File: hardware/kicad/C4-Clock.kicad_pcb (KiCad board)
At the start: 2 copper layers, 99 x 99 mm, 39 parts, among them J1 Keypad, J2 Battery, J3 LCD1602, J4 Boost Module, J5 ICSP, K1 FINDER-36.11-5V, Q1 S9014, Q2 S9014, Q3 S9014, SW1 SW_SPST, SW2 SW_SPST, U1 ATmega328P-P, U2 AMS1117-5.0, U3 PCF8574A, U4 DS1302+, Y1 16MHz, Y2 32.768kHz

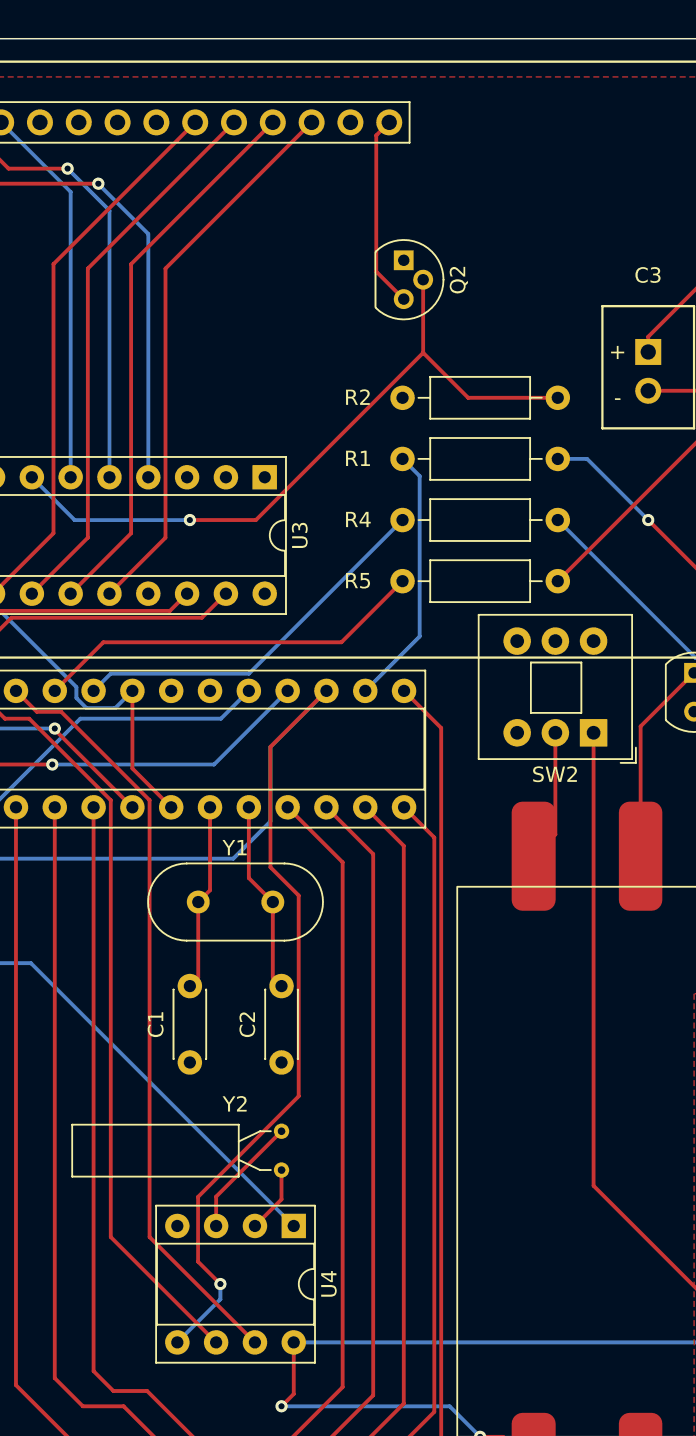
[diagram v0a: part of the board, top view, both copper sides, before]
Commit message: kicad: Remove unused pin A0
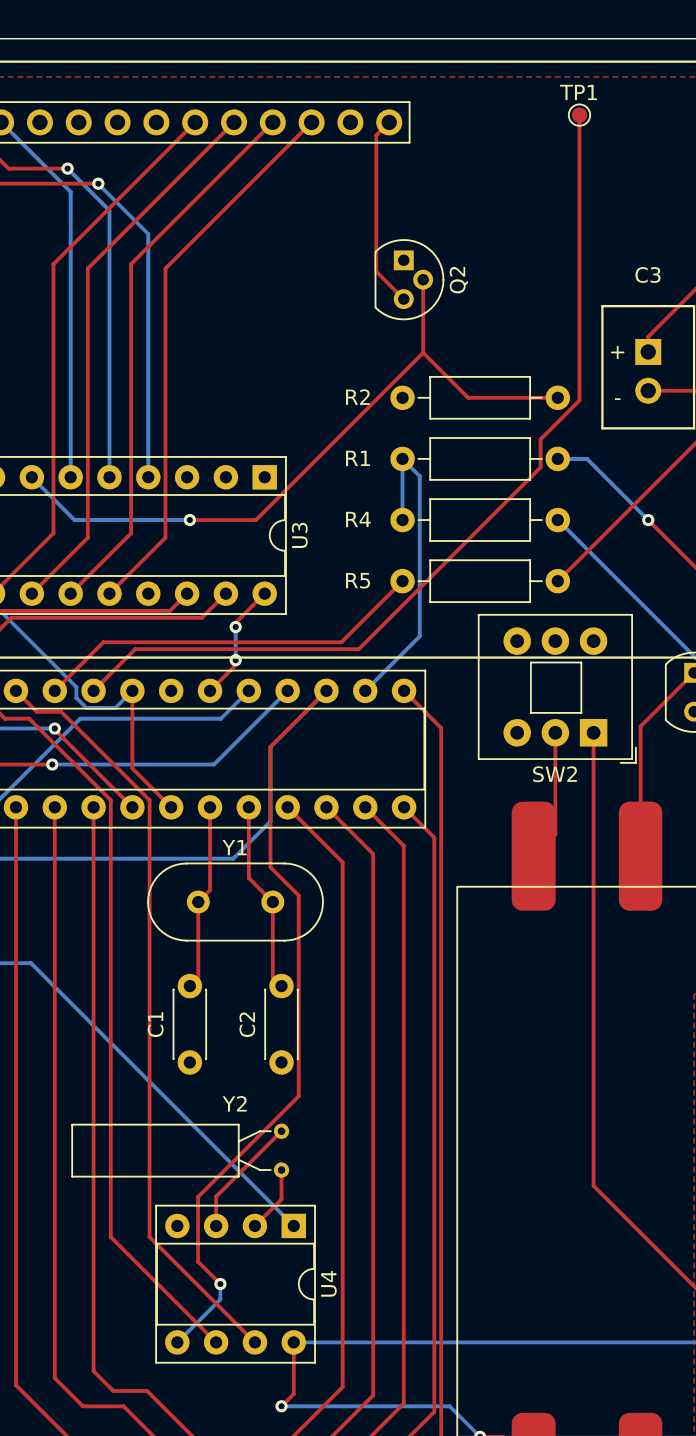
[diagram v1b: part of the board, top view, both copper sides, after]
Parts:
- added TP1: RandomSeed, TestPoint:TestPoint_Pad_D1.0mm, F.Cu at (144.5, 44.5)
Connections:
- R4 pad 1: LED -> BUZZER
- U1 pad 23: LED -> Net-(TP1-Pad1)
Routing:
- net Net-(TP1-Pad1): track 0.00 -> 61.0 mm
- net LED: track 24.9 -> 0.00 mm
- net +5V: track 111.8 -> 119.6 mm, vias 4 -> 6
- net BUZZER: track 17.1 -> 21.1 mm
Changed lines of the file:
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@@
   (net 35 "Net-(Q2-Pad2)")
   (net 36 "BUZZER")
-  (net 37 "LED")
+  (net 37 "Net-(TP1-Pad1)")
   (net 38 "Net-(SW1-Pad2)")
   (net 39 "Net-(BT1-Pad1)")
@@
     (fp_line (start 8.23 1.25) (end 8.23 -1.25) (layer "F.Fab") (width 0.1))
     (pad "1" thru_hole circle (at 0 0) (size 1.6 1.6) (drill 0.8) (layers *.Cu *.Mask)
-      (net 37 "LED") (pintype "passive"))
+      (net 36 "BUZZER") (pintype "passive"))
     (pad "2" thru_hole oval (at 10.16 0) (size 1.6 1.6) (drill 0.8) (layers *.Cu *.Mask)
       (net 7 "Net-(D1-Pad2)") (pintype "passive"))
@@
       (net 3 "GND") (pinfunction "GND") (pintype "passive"))
     (pad "23" thru_hole oval (at 7.62 12.7 90) (size 1.6 1.6) (drill 0.8) (layers *.Cu *.Mask)
-      (net 37 "LED") (pinfunction "PC0") (pintype "bidirectional"))
+      (net 37 "Net-(TP1-Pad1)") (pinfunction "PC0") (pintype "bidirectional"))
     (pad "24" thru_hole oval (at 7.62 10.16 90) (size 1.6 1.6) (drill 0.8) (layers *.Cu *.Mask)
       (net 8 "RELAY") (pinfunction "PC1") (pintype "bidirectional"))
@@
       (rotate (xyz 0 0 0))
     )
+  )
+  (footprint "TestPoint:TestPoint_Pad_D1.0mm" (layer "F.Cu")
+    (at 144.5 44.5)
+    (descr "SMD pad as test Point, diameter 1.0mm")
+    (tags "test point SMD pad")
+    (property "Sheetfile" "C4-Clock.kicad_sch")
+    (property "Sheetname" "")
+    (attr exclude_from_pos_files)
+    (fp_text reference "TP1" (at 0 -1.448) (layer "F.SilkS")
+      (effects (font (size 1 1) (thickness 0.15)))
+    )
+    (fp_text value "RandomSeed" (at 0 1.55) (layer "F.Fab")
+      (effects (font (size 1 1) (thickness 0.15)))
+    )
+    (fp_text user "${REFERENCE}" (at 0 -1.45) (layer "F.Fab")
+      (effects (font (size 1 1) (thickness 0.15)))
+    )
+    (fp_circle (center 0 0) (end 0 0.7) (layer "F.SilkS") (width 0.12) (fill none))
+    (fp_circle (center 0 0) (end 1 0) (layer "F.CrtYd") (width 0.05) (fill none))
+    (pad "1" smd circle (at 0 0) (size 1 1) (layers "F.Cu" "F.Mask")
+      (net 37 "Net-(TP1-Pad1)") (pinfunction "1") (pintype "passive"))
   )
   (footprint "Potentiometer_THT:Potentiometer_Vishay_T73YP_Vertical" (layer "F.Cu")
@@
   (segment (start 162.824511 118.705738) (end 158.530249 123) (width 0.25) (layer "F.Cu") (net 1))
   (segment (start 138 131) (end 139.5 131) (width 0.25) (layer "F.Cu") (net 1))
+  (segment (start 122 80.17402) (end 122 80.5) (width 0.25) (layer "F.Cu") (net 1))
+  (segment (start 122 77.72) (end 122 78) (width 0.25) (layer "F.Cu") (net 1))
   (segment (start 110.16 84.72) (end 110.16 84.645102) (width 0.25) (layer "F.Cu") (net 1))
+  (segment (start 122 80.5) (end 120.32 82.18) (width 0.25) (layer "F.Cu") (net 1))
   (segment (start 139.5 131) (end 141.5 133) (width 0.25) (layer "F.Cu") (net 1))
   (segment (start 125.8 128.2) (end 125 129) (width 0.25) (layer "F.Cu") (net 1))
   (segment (start 162.824511 99.624511) (end 162.824511 118.705738) (width 0.25) (layer "F.Cu") (net 1))
   (segment (start 158.530249 123) (end 155 123) (width 0.25) (layer "F.Cu") (net 1))
+  (segment (start 123.9 75.82) (end 122 77.72) (width 0.25) (layer "F.Cu") (net 1))
   (segment (start 162.2 99) (end 162.824511 99.624511) (width 0.25) (layer "F.Cu") (net 1))
   (segment (start 115.24 89.8) (end 110.16 84.72) (width 0.25) (layer "F.Cu") (net 1))
   (via (at 125 129) (size 0.8) (drill 0.4) (layers "F.Cu" "B.Cu") (net 1))
+  (via (at 122 80.17402) (size 0.8) (drill 0.4) (layers "F.Cu" "B.Cu") (net 1))
+  (via (at 122 78) (size 0.8) (drill 0.4) (layers "F.Cu" "B.Cu") (net 1))
   (via (at 138 131) (size 0.8) (drill 0.4) (layers "F.Cu" "B.Cu") (net 1))
   (via (at 110.16 84.645102) (size 0.8) (drill 0.4) (layers "F.Cu" "B.Cu") (net 1))
@@
   (segment (start 110.16 84.645102) (end 90.145102 84.645102) (width 0.25) (layer "B.Cu") (net 1))
   (segment (start 90.145102 84.645102) (end 88.5 83) (width 0.25) (layer "B.Cu") (net 1))
+  (segment (start 122 78) (end 122 80.17402) (width 0.25) (layer "B.Cu") (net 1))
   (segment (start 155 123) (end 153.18 124.82) (width 0.25) (layer "B.Cu") (net 1))
   (segment (start 154.34 83.54) (end 169.8 99) (width 0.25) (layer "B.Cu") (net 2))
@@
   (segment (start 134.044511 68.124511) (end 134.044511 78.615489) (width 0.25) (layer "B.Cu") (net 36))
   (segment (start 134.044511 78.615489) (end 130.48 82.18) (width 0.25) (layer "B.Cu") (net 36))
+  (segment (start 132.92 67) (end 132.92 71) (width 0.25) (layer "B.Cu") (net 36))
   (segment (start 132.92 67) (end 134.044511 68.124511) (width 0.25) (layer "B.Cu") (net 36))
-  (segment (start 122.864511 81.055489) (end 132.92 71) (width 0.25) (layer "B.Cu") (net 37))
-  (segment (start 113.824511 81.055489) (end 122.864511 81.055489) (width 0.25) (layer "B.Cu") (net 37))
+  (segment (start 144.5 45) (end 144.5 44.5) (width 0.25) (layer "F.Cu") (net 37))
+  (segment (start 115.43048 79.44952) (end 130.06078 79.44952) (width 0.25) (layer "F.Cu") (net 37))
+  (segment (start 144.5 63.1703) (end 144.5 45) (width 0.25) (layer "F.Cu") (net 37))
+  (segment (start 141.955489 65.714811) (end 144.5 63.1703) (width 0.25) (layer "F.Cu") (net 37))
+  (segment (start 141.955489 67.554811) (end 141.955489 65.714811) (width 0.25) (layer "F.Cu") (net 37))
+  (segment (start 130.06078 79.44952) (end 141.955489 67.554811) (width 0.25) (layer "F.Cu") (net 37))
+  (segment (start 112.7 82.18) (end 115.43048 79.44952) (width 0.25) (layer "F.Cu") (net 37))
   (segment (start 112.7 82.18) (end 113.824511 81.055489) (width 0.25) (layer "B.Cu") (net 37))
   (segment (start 86.6425 68.0925) (end 94.85 76.3) (width 0.25) (layer "F.Cu") (net 38))
@@
   (segment (start 121.840489 93.159511) (end 124.275489 90.724511) (width 0.25) (layer "B.Cu") (net 45))
   (segment (start 108.99048 83.55048) (end 110.58078 83.55048) (width 0.25) (layer "F.Cu") (net 46))
-  (segment (start 116.364511 117.924511) (end 123.26 124.82) (width 0.25) (layer "F.Cu") (net 46))
+  (segment (start 123.26 124.82) (end 116.364511 117.924511) (width 0.25) (layer "F.Cu") (net 46))
   (segment (start 107.62 82.18) (end 108.99048 83.55048) (width 0.25) (layer "F.Cu") (net 46))
   (segment (start 116.364511 89.334211) (end 116.364511 117.924511) (width 0.25) (layer "F.Cu") (net 46))

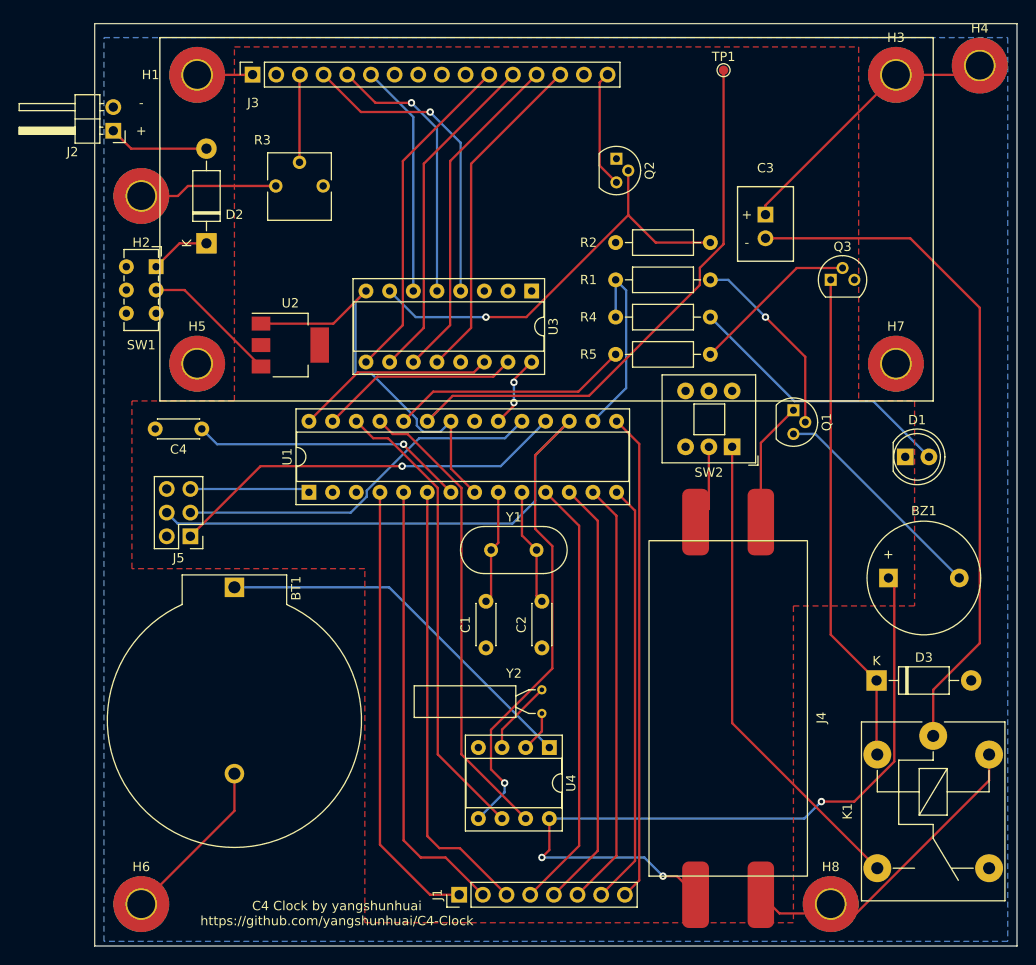
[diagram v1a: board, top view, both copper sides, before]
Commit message: kicad: Change ATmega328P to ESP32-WROOM-32
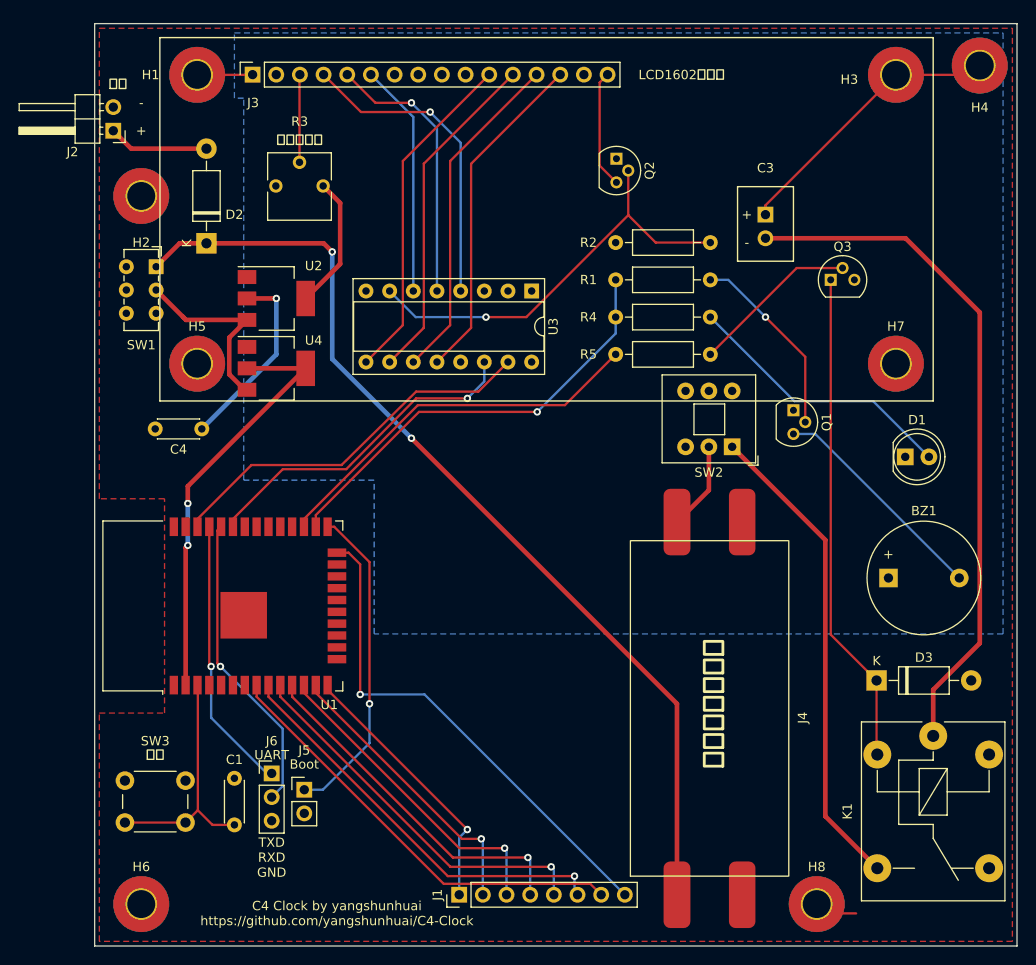
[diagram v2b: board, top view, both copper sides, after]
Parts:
- removed BT1: CR2032, Battery:BatteryHolder_ComfortableElectronic_CH273-2450_1x2450
- removed C2: 22pF, Capacitor_THT:C_Disc_D4.3mm_W1.9mm_P5.00mm
- removed TP1: RandomSeed, TestPoint:TestPoint_Pad_D1.0mm
- removed Y1: 16MHz, Crystal:Crystal_HC49-4H_Vertical
- removed Y2: 32.768kHz, Crystal:Crystal_AT310_D3.0mm_L10.0mm_Horizontal
- added J6: Debug, Connector_PinHeader_2.54mm:PinHeader_1x03_P2.54mm_Vertical, F.Cu at (96.0, 120.0)
- added SW3: Reset, Button_Switch_THT:SW_PUSH_6mm_H5mm, F.Cu at (80.2, 120.8)
- C1: value 22pF -> 0.1uF
- J5: value ICSP -> Boot; footprint Connector_PinHeader_2.54mm:PinHeader_2x03_P2.54mm_Vertical -> Connector_PinHeader_2.54mm:PinHeader_1x02_P2.54mm_Vertical
- U1: value ATmega328P-P -> ESP32-WROOM-32D; footprint Package_DIP:DIP-28_W7.62mm_Socket -> RF_Module:ESP32-WROOM-32
- U4: value DS1302+ -> AMS1117-3.3; footprint Package_DIP:DIP-8_W7.62mm_Socket -> Package_TO_SOT_SMD:SOT-223-3_TabPin2
- moved U4 50.1 mm to (96.5, 76.5), turned to 0 degrees
- moved C1 30.4 mm to (92.0, 120.5), turned to -90 degrees
- moved J5 29.8 mm to (99.5, 121.7), turned to 0 degrees
- moved U1 13.7 mm to (93.8, 102.0)
- moved U2 5.22 mm to (96.5, 69.0)
- moved J4 2.00 mm to (147.5, 114.0)
- moved H8 1.50 mm to (154.5, 134.0)
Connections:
- J4 pad 1: +5V -> +8V
- J5 pad 1: PB4 -> Net-(J5-Pad1)
- J5 pad 2: +5V -> GND
- U1 pad 1: RESET -> GND
- U1 pad 10: Net-(C2-Pad2) -> Net-(J1-Pad5)
- U1 pad 12: Net-(J1-Pad5) -> Net-(J1-Pad3)
- U1 pad 13: Net-(J1-Pad6) -> Net-(J1-Pad2)
- U1 pad 14: Net-(J1-Pad7) -> Net-(J1-Pad1)
- U1 pad 15: Net-(J1-Pad8) -> GND
- U1 pad 16: BUZZER -> unconnected-(U1-Pad16)
- U1 pad 17: PB3 -> unconnected-(U1-Pad17)
- U1 pad 18: PB4 -> unconnected-(U1-Pad18)
- U1 pad 19: PB5 -> unconnected-(U1-Pad19)
- U1 pad 2: unconnected-(U1-Pad2) -> +3V3
- U1 pad 20: +5V -> unconnected-(U1-Pad20)
- U1 pad 22: GND -> unconnected-(U1-Pad22)
- U1 pad 23: Net-(TP1-Pad1) -> unconnected-(U1-Pad23)
- U1 pad 24: RELAY -> Net-(J1-Pad8)
- U1 pad 25: DS1302_CLK -> Net-(J5-Pad1)
- U1 pad 26: DS1302_IO -> BUZZER
- U1 pad 27: Net-(U1-Pad27) -> RELAY
- U1 pad 28: Net-(U1-Pad28) -> unconnected-(U1-Pad28)
- U1 pad 3: unconnected-(U1-Pad3) -> Net-(C1-Pad2)
- U1 pad 4: Net-(J1-Pad1) -> unconnected-(U1-Pad4)
- U1 pad 5: Net-(J1-Pad2) -> unconnected-(U1-Pad5)
- U1 pad 6: Net-(J1-Pad3) -> unconnected-(U1-Pad6)
- U1 pad 7: +5V -> unconnected-(U1-Pad7)
- U1 pad 8: GND -> Net-(J1-Pad7)
- U1 pad 9: Net-(C1-Pad2) -> Net-(J1-Pad6)
- U3 pad 14: Net-(U1-Pad28) -> Net-(U1-Pad33)
- U3 pad 15: Net-(U1-Pad27) -> Net-(U1-Pad36)
- U4 pad 1: Net-(BT1-Pad1) -> GND
- U4 pad 2: Net-(U4-Pad2) -> +3V3
- U4 pad 3: Net-(U4-Pad3) -> Net-(SW1-Pad2)
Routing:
- net GND: track 162.1 -> 38.9 mm
- net PB3: track 100.5 -> 0.00 mm, vias 1 -> 0
- net +8V: track 6.44 -> 104.6 mm, vias 0 -> 2
- net +5V: track 119.6 -> 34.8 mm, vias 6 -> 1
- net Net-(TP1-Pad1): track 61.0 -> 0.00 mm
- net DS1302_CLK: track 50.6 -> 0.00 mm
- net DS1302_IO: track 50.0 -> 0.00 mm
- net +3V3: track 0.00 -> 45.6 mm, vias 0 -> 2
- net PB4: track 43.2 -> 0.00 mm, vias 1 -> 0
- net Net-(U1-Pad36): track 0.00 -> 41.1 mm
- net Net-(BT1-Pad1): track 40.9 -> 0.00 mm
- net PB5: track 40.0 -> 0.00 mm
- net Net-(U1-Pad33): track 0.00 -> 36.0 mm, vias 0 -> 1
- net Net-(J5-Pad1): track 0.00 -> 34.6 mm, vias 0 -> 1
- net RXD: track 0.00 -> 32.6 mm, vias 0 -> 1
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- added copper zone on B.Cu, net +5V
- added copper zone on F.Cu, net GND
- removed copper zone on F.Cu, net +5V
- removed copper zone on B.Cu, net GND
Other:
- board text added: "Boot"
- board text added: "LCD1602安装处"
- board text added: "TXD RXD GND"
- board text added: "UART"
- board text added: "升压模块安装处"
- board text added: "复位"
- board text added: "对比度调节"
- board text added: "电池"
